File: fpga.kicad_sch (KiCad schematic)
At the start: 16 parts, among them U11 TLV77512PDBVR, U13 TLV77533PDBVR, U2 ICE40LP1K-CM36

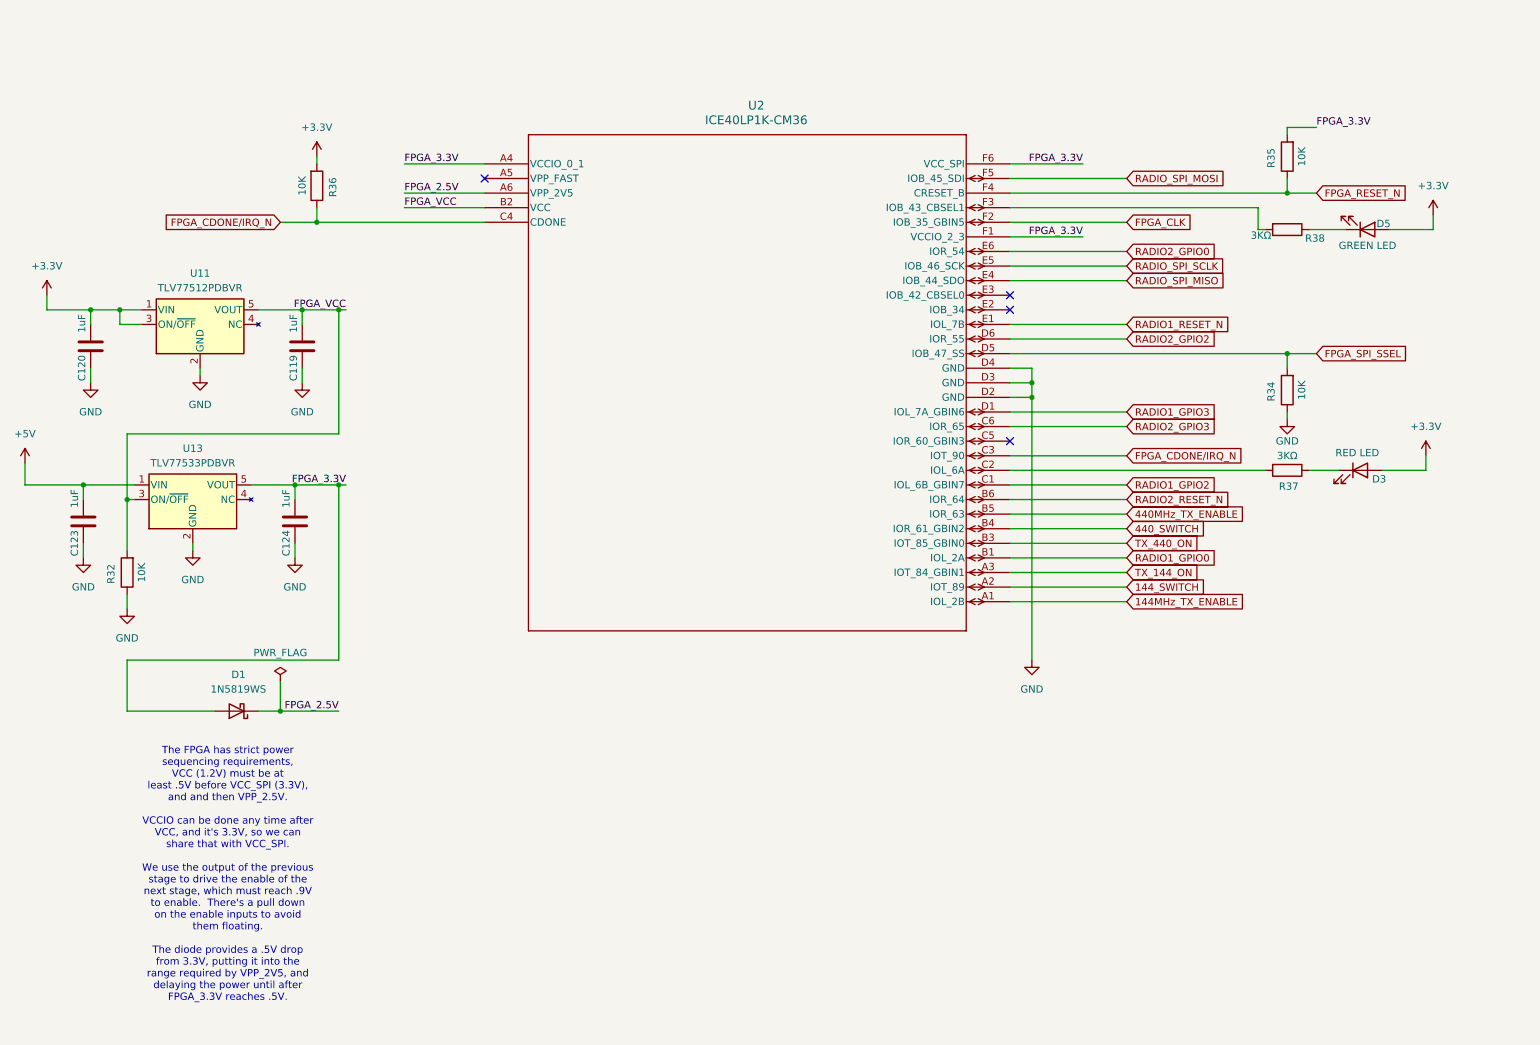
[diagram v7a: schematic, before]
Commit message: Replace the FPGA with a QFP one
It has more pins, which might be useful, and it's easier to work with
than the BGA.  It also has a built-in SPI.  It's currently an ICE40UP5K,
but the ICE5LP[124]K chips are pin compatible and cheaper.

Signed-off-by: Corey Minyard <corey@minyard.net>
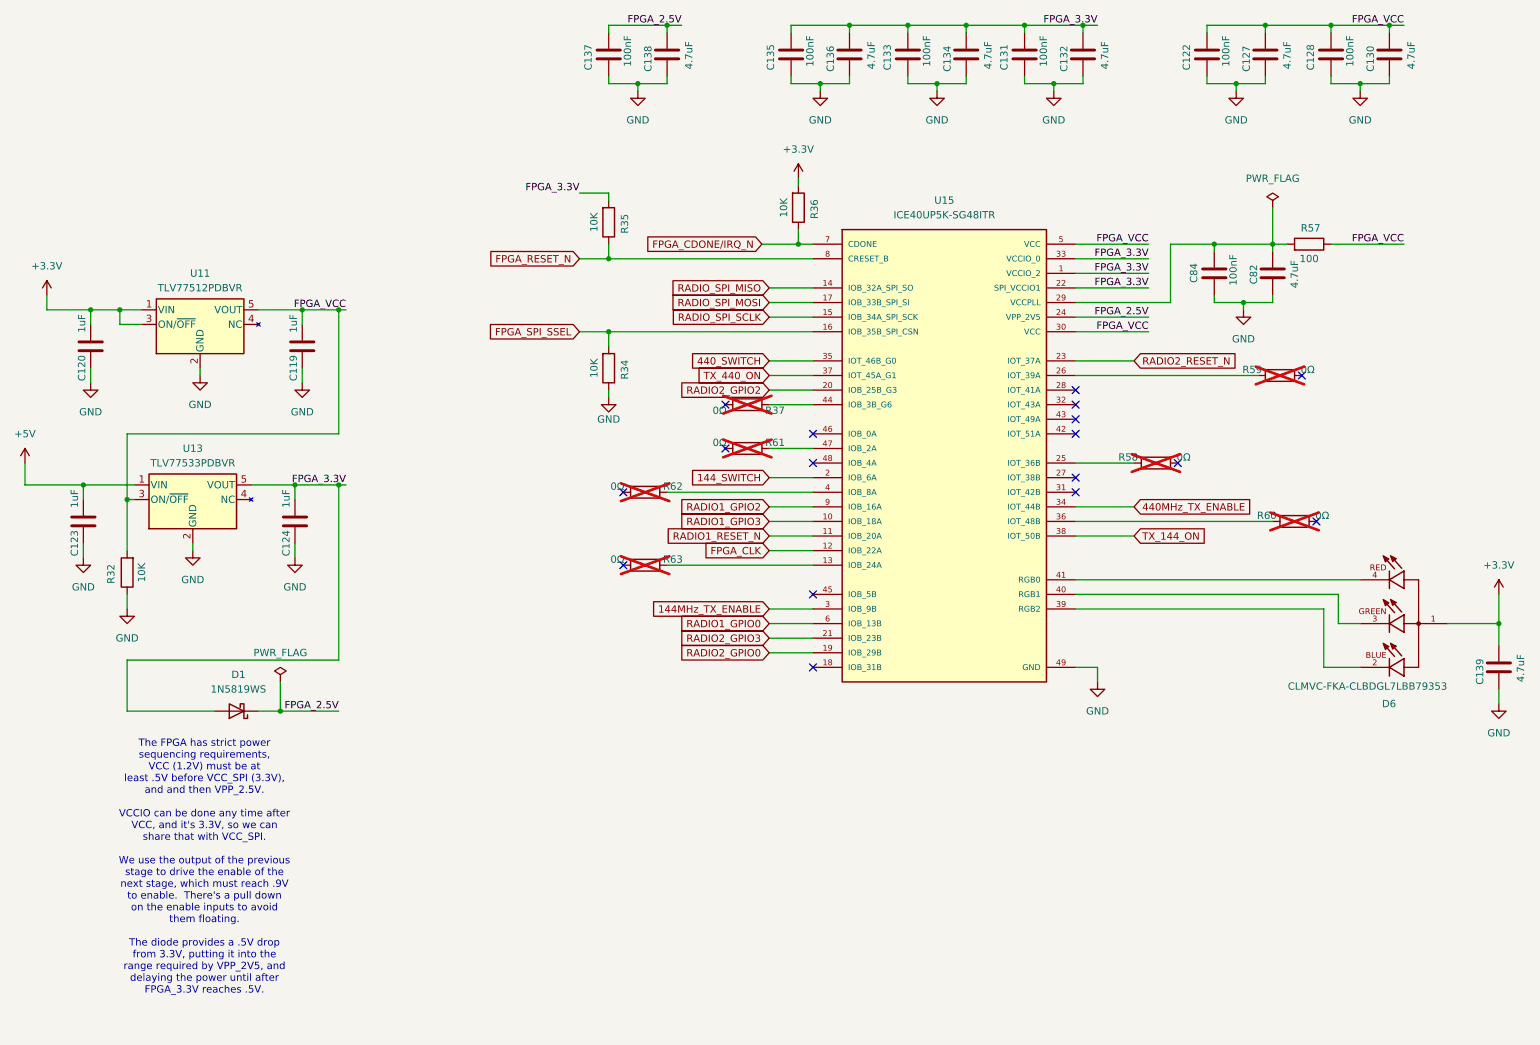
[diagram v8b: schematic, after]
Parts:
- removed D3: RED LED, LED_SMD:LED_0603_1608Metric_Pad1.05x0.95mm_HandSolder, symbol Device:LED
- removed D5: GREEN LED, LED_SMD:LED_0603_1608Metric_Pad1.05x0.95mm_HandSolder, symbol Device:LED
- removed R38: 3KΩ, Resistor_SMD:R_0603_1608Metric_Pad0.98x0.95mm_HandSolder, symbol Device:R
- removed U2: ICE40LP1K-CM36, footprints:UCBGA36_LAT, symbol Local ICs:ICE40LP1K-CM36
- added C122, C128, C131, C133, C135, C137, C84: 100nF, Capacitor_SMD:C_0402_1005Metric_Pad0.74x0.62mm_HandSolder, symbol Device:C
- added C127, C130, C132, C134, C136, C138, C139, C82: 4.7uF, Capacitor_SMD:C_0603_1608Metric_Pad1.08x0.95mm_HandSolder, symbol Device:C
- added D6: CLMVC-FKA-CLBDGL7LBB79353, footprints:LED_CLMVC-FKA-CLBDGL7LBB79353, symbol Local ICs:CLMVC-FKA-CLBDGL7LBB79353
- added R57: 100, Resistor_SMD:R_0402_1005Metric, symbol Device:R
- added R58, R59, R60, R61, R62, R63: 0Ω, Resistor_SMD:R_0402_1005Metric_Pad0.72x0.64mm_HandSolder, symbol Device:R
- added U15: ICE40UP5K-SG48ITR, footprints:QFN50P700X700X100-49N, symbol ICs:ICE40UP5K-SG48ITR
- R37: value 3KΩ -> 0Ω; footprint Resistor_SMD:R_0603_1608Metric_Pad0.98x0.95mm_HandSolder -> Resistor_SMD:R_0402_1005Metric_Pad0.72x0.64mm_HandSolder; now not fitted; now left out of the parts list
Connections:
- net +3.3V: now also C139.2, D6.1
- net 144MHz_TX_ENABLE: now also U15.3 (IOB_9B)
- net 144_SWITCH: now also U15.2 (IOB_6A)
- net 440MHz_TX_ENABLE: now also U15.34 (IOT_44B)
- net 440_SWITCH: now also U15.35 (IOT_46B_G0)
- net FPGA_2.5V: now also C137.2, C138.2, U15.24 (VPP_2V5)
- net FPGA_3.3V: now also C131.2, C132.2, C133.2, C134.2, C135.2, C136.2, U15.1 (VCCIO_2), U15.22 (SPI_VCCIO1), U15.33 (VCCIO_0)
- net FPGA_CDONE/IRQ_N: now also U15.7 (CDONE)
- net FPGA_CLK: now also U15.12 (IOB_22A)
- net FPGA_RESET_N: now also U15.8 (CRESET_B)
- net FPGA_SPI_SSEL: now also U15.16 (IOB_35B_SPI_CSN)
- net FPGA_VCC: now also C122.2, C127.2, C128.2, C130.2, R57.1, U15.30 (VCC), U15.5 (VCC)
- net GND: now also C122.1, C127.1, C128.1, C130.1, C131.1, C132.1, C133.1, C134.1, C135.1, C136.1, C137.1, C138.1, C139.1, C82.1, C84.1, U15.49 (GND)
- net RADIO1_GPIO0: now also U15.6 (IOB_13B)
- net RADIO1_GPIO2: now also U15.9 (IOB_16A)
- net RADIO1_GPIO3: now also U15.10 (IOB_18A)
- net RADIO1_RESET_N: now also U15.11 (IOB_20A)
- net RADIO2_GPIO0: now also U15.19 (IOB_29B)
- net RADIO2_GPIO2: now also U15.20 (IOB_25B_G3)
- net RADIO2_GPIO3: now also U15.21 (IOB_23B)
- net RADIO2_RESET_N: now also U15.23 (IOT_37A)
- net RADIO_SPI_MISO: now also U15.14 (IOB_32A_SPI_SO)
- net RADIO_SPI_MOSI: now also U15.17 (IOB_33B_SPI_SI)
- net RADIO_SPI_SCLK: now also U15.15 (IOB_34A_SPI_SCK)
- net TX_144_ON: now also U15.38 (IOT_50B)
- net TX_440_ON: now also U15.37 (IOT_45A_G1)
- net at R37.1: now also U15.44 (IOB_3B_G6)
- new net: R61.1, U15.47 (IOB_2A)
- new net: R63.1, U15.13 (IOB_24A)
- new net: R62.1, U15.4 (IOB_8A)
- new net: R58.1, U15.25 (IOT_36B)
- new net: R59.1, U15.26 (IOT_39A)
- new net: C82.2, C84.2, R57.2, U15.29 (VCCPLL)
- new net: R60.1, U15.36 (IOT_48B)
- new net: D6.2, U15.39 (RGB2)
- new net: D6.3, U15.40 (RGB1)
- new net: D6.4, U15.41 (RGB0)
- no-connect marks 4 -> 17
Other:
- moved on the sheet: R34, R35, R36
